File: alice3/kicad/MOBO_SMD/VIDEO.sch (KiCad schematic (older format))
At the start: 19 parts, among them P1 CONN_01X05, SW1 RESET, U2 Propeller_P8X32A-D40, U3 24LC256, U4 Propeller_Plug, Y1 5 MHz

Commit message: Unknown wiring changes automatically done by KiCAD in video board as a result of adding the EEPROM.
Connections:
- wire segments 134 -> 118
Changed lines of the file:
@@
 LIBS:mini_din
 LIBS:24lc256
+LIBS:MOBO_SMD-cache
 EELAYER 25 0
 EELAYER END
@@
 	3800 3550 3700 3550
 Wire Wire Line
-	3700 3550 3700 3650
-Wire Wire Line
-	3700 3650 3700 3850
+	3700 3550 3700 3850
 Wire Wire Line
 	3800 3650 3700 3650
@@
 	3700 1550 3800 1550
 Wire Wire Line
-	3700 1250 3700 1450
-Wire Wire Line
-	3700 1450 3700 1550
+	3700 1250 3700 1550
 Wire Wire Line
 	3800 1450 3700 1450
@@
 	5000 1550 5050 1550
 Wire Wire Line
-	5000 1450 5400 1450
-Wire Wire Line
-	5400 1450 5450 1450
-Wire Wire Line
-	5450 1450 5600 1450
+	5000 1450 5600 1450
 Wire Wire Line
 	3100 2650 3800 2650
@@
 	6000 3150 5950 3150
 Wire Wire Line
-	5950 3150 5950 3250
-Wire Wire Line
-	5950 3250 5950 3350
-Wire Wire Line
-	5950 3350 5950 3450
-Wire Wire Line
-	5950 3450 5950 3550
+	5950 3150 5950 3550
 Wire Wire Line
 	6000 3250 5950 3250
@@
 	7050 3450 7050 3850
 Wire Wire Line
-	7050 3850 5700 3850
-Wire Wire Line
-	5700 3850 5700 3150
-Wire Wire Line
-	5700 3150 5700 3100
+	5700 3850 7050 3850
+Wire Wire Line
+	5700 3100 5700 3850
 Wire Wire Line
 	5700 3150 5000 3150
@@
 	6850 1450 6850 1850
 Wire Wire Line
-	6200 1450 6250 1450
-Wire Wire Line
-	6250 1450 6850 1450
+	6200 1450 6850 1450
 Wire Wire Line
 	6250 1450 6250 1550
@@
 	3325 6225 3450 6225
 Wire Wire Line
-	3325 5725 3325 5825
-Wire Wire Line
-	3325 5825 3325 6225
-Wire Wire Line
-	3325 6225 3325 6425
-Wire Wire Line
-	3325 6425 3325 6625
-Wire Wire Line
-	3325 6625 3325 6775
+	3325 5725 3325 6775
 Wire Wire Line
 	3450 6425 3325 6425
@@
 	1800 6575 2325 6575
 Wire Wire Line
-	2325 6525 2325 6575
-Wire Wire Line
-	2325 6575 2325 6750
+	2325 6525 2325 6750
 Wire Wire Line
 	2325 6525 3450 6525
 Wire Wire Line
-	2325 6225 2325 6325
-Wire Wire Line
-	2325 6325 2325 6400
+	2325 6225 2325 6400
 Wire Wire Line
 	2325 6325 3450 6325
@@
 	1800 5875 2325 5875
 Wire Wire Line
-	2325 5875 2325 6050
-Wire Wire Line
-	2325 6050 2325 6125
+	2325 5875 2325 6125
 Wire Wire Line
 	2325 6400 1800 6400

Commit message: Fix up various small things.
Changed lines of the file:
@@
 	7050 3450 7050 3850
 Wire Wire Line
-	5700 3850 7050 3850
+	7050 3850 5700 3850
 Wire Wire Line
-	5700 3100 5700 3850
+	5700 3850 5700 3100
 Wire Wire Line
 	5700 3150 5000 3150

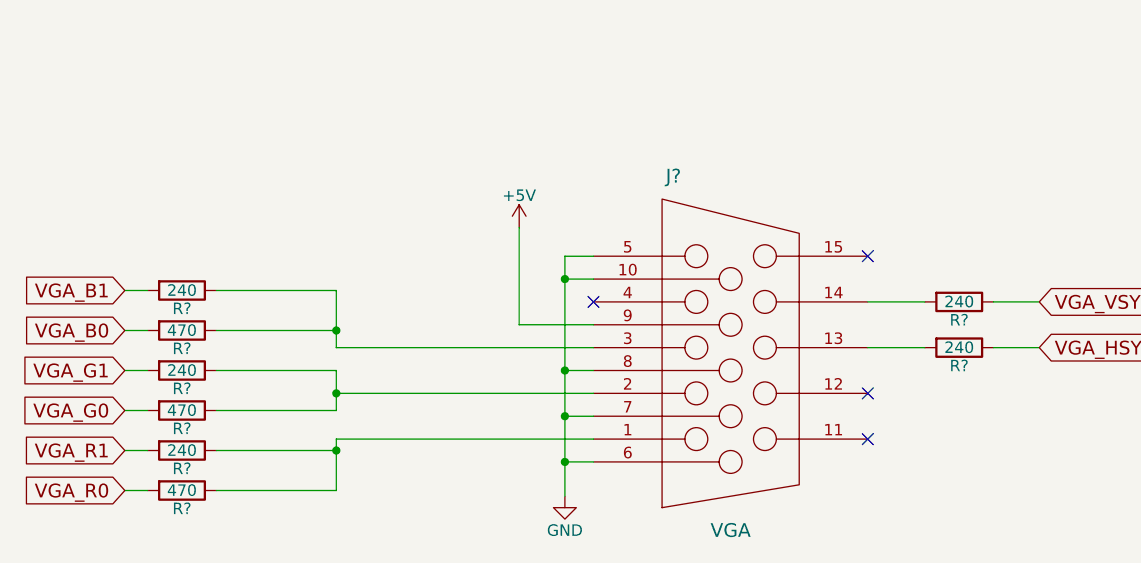
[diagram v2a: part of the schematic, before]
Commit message: Assign part names.
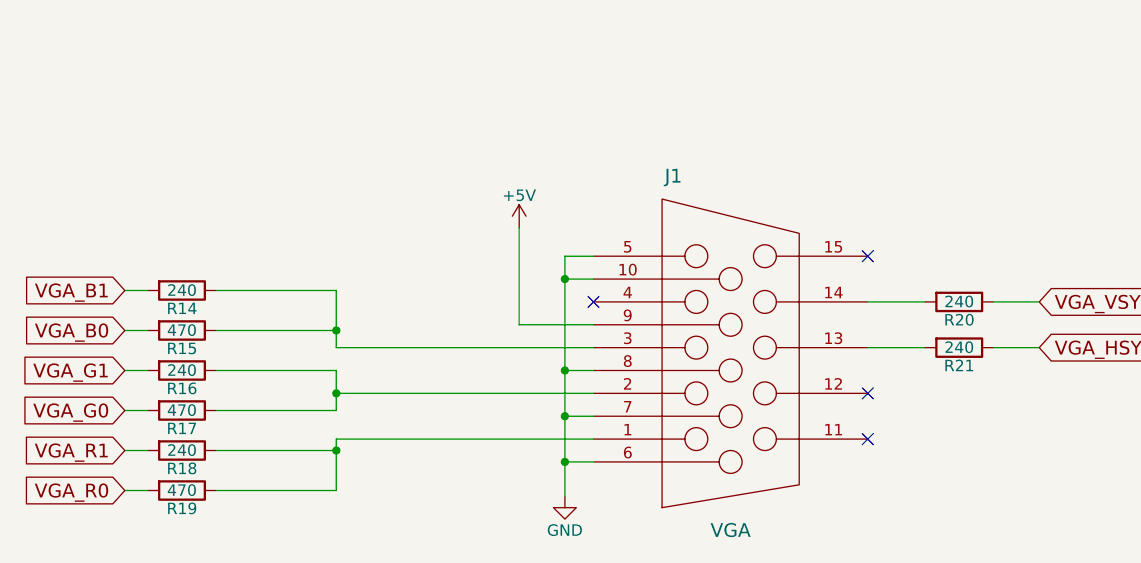
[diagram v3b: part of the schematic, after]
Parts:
- gave numbers to parts that had none: 9
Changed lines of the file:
@@
 $EndComp
 $Comp
-L GND #PWR01
+L GND #PWR9
 U 1 1 566E4A0D
 P 3700 3850
-F 0 "#PWR01" H 3700 3600 50  0001 C CNN
+F 0 "#PWR9" H 3700 3600 50  0001 C CNN
 F 1 "GND" H 3700 3700 50  0000 C CNN
 F 2 "" H 3700 3850 50  0000 C CNN
@@
 $EndComp
 $Comp
-L +3.3V #PWR02
+L +3.3V #PWR8
 U 1 1 566E4A37
 P 3700 1250
-F 0 "#PWR02" H 3700 1100 50  0001 C CNN
+F 0 "#PWR8" H 3700 1100 50  0001 C CNN
 F 1 "+3.3V" H 3700 1390 50  0000 C CNN
 F 2 "" H 3700 1250 50  0000 C CNN
@@
 $EndComp
 $Comp
-L GND #PWR03
+L GND #PWR13
 U 1 1 566E4C07
 P 6250 1550
-F 0 "#PWR03" H 6250 1300 50  0001 C CNN
+F 0 "#PWR13" H 6250 1300 50  0001 C CNN
 F 1 "GND" H 6250 1400 50  0000 C CNN
 F 2 "" H 6250 1550 50  0000 C CNN
@@
 $EndComp
 $Comp
-L GND #PWR04
+L GND #PWR12
 U 1 1 5681F164
 P 5950 3550
-F 0 "#PWR04" H 5950 3300 50  0001 C CNN
+F 0 "#PWR12" H 5950 3300 50  0001 C CNN
 F 1 "GND" H 5950 3400 50  0000 C CNN
 F 2 "" H 5950 3550 50  0000 C CNN
@@
 $EndComp
 $Comp
-L +3.3V #PWR05
+L +3.3V #PWR14
 U 1 1 5681F2C2
 P 7050 3000
-F 0 "#PWR05" H 7050 2850 50  0001 C CNN
+F 0 "#PWR14" H 7050 2850 50  0001 C CNN
 F 1 "+3.3V" H 7050 3140 50  0000 C CNN
 F 2 "" H 7050 3000 50  0000 C CNN
@@
 $EndComp
 $Comp
-L GND #PWR06
+L GND #PWR15
 U 1 1 5681F2E8
 P 7300 3300
-F 0 "#PWR06" H 7300 3050 50  0001 C CNN
+F 0 "#PWR15" H 7300 3050 50  0001 C CNN
 F 1 "GND" H 7300 3150 50  0000 C CNN
 F 2 "" H 7300 3300 50  0000 C CNN
@@
 $EndComp
 $Comp
-L +3.3V #PWR07
+L +3.3V #PWR11
 U 1 1 5681F435
 P 5700 2750
-F 0 "#PWR07" H 5700 2600 50  0001 C CNN
+F 0 "#PWR11" H 5700 2600 50  0001 C CNN
 F 1 "+3.3V" H 5700 2890 50  0000 C CNN
 F 2 "" H 5700 2750 50  0000 C CNN
@@
 $EndComp
 $Comp
-L GND #PWR08
+L GND #PWR3
 U 1 1 56821F3F
 P 2700 1850
-F 0 "#PWR08" H 2700 1600 50  0001 C CNN
+F 0 "#PWR3" H 2700 1600 50  0001 C CNN
 F 1 "GND" H 2700 1700 50  0000 C CNN
 F 2 "" H 2700 1850 50  0000 C CNN
@@
 $EndComp
 $Comp
-L GND #PWR09
+L GND #PWR10
 U 1 1 56826035
 P 5050 1550
-F 0 "#PWR09" H 5050 1300 50  0001 C CNN
+F 0 "#PWR10" H 5050 1300 50  0001 C CNN
 F 1 "GND" H 5050 1400 50  0000 C CNN
 F 2 "" H 5050 1550 50  0000 C CNN
@@
 $EndComp
 $Comp
-L GND #PWR012
+L GND #PWR7
 U 1 1 568DD571
 P 3400 1350
-F 0 "#PWR012" H 3400 1100 50  0001 C CNN
+F 0 "#PWR7" H 3400 1100 50  0001 C CNN
 F 1 "GND" H 3400 1200 50  0000 C CNN
 F 2 "" H 3400 1350 50  0000 C CNN
@@
 $EndComp
 $Comp
-L +3.3V #PWR013
+L +3.3V #PWR6
 U 1 1 568DD5A9
 P 3400 850
-F 0 "#PWR013" H 3400 700 50  0001 C CNN
+F 0 "#PWR6" H 3400 700 50  0001 C CNN
 F 1 "+3.3V" H 3400 990 50  0000 C CNN
 F 2 "" H 3400 850 50  0000 C CNN
@@
 $EndComp
 $Comp
-L GND #PWR014
+L GND #PWR1
 U 1 1 56A0506B
 P 1000 3050
-F 0 "#PWR014" H 1000 2800 50  0001 C CNN
+F 0 "#PWR1" H 1000 2800 50  0001 C CNN
 F 1 "GND" H 1000 2900 50  0000 C CNN
 F 2 "" H 1000 3050 50  0000 C CNN
@@
 $EndComp
 $Comp
-L +3.3V #PWR015
+L +3.3V #PWR2
 U 1 1 56A050A3
 P 1300 3050
-F 0 "#PWR015" H 1300 2900 50  0001 C CNN
+F 0 "#PWR2" H 1300 2900 50  0001 C CNN
 F 1 "+3.3V" H 1300 3190 50  0000 C CNN
 F 2 "" H 1300 3050 50  0000 C CNN
@@
 	1000 2950 1000 3050
 $Comp
-L VGA J?
+L VGA J1
 U 1 1 56CDDE3D
 P 4050 6175
-F 0 "J?" H 3800 6975 60  0000 C CNN
+F 0 "J1" H 3800 6975 60  0000 C CNN
 F 1 "VGA" H 4050 5425 60  0000 C CNN
 F 2 "" H 4050 6175 60  0000 C CNN
@@
 $EndComp
 $Comp
-L GND #PWR?
+L GND #PWR5
 U 1 1 56CDE065
 P 3325 6775
-F 0 "#PWR?" H 3325 6525 50  0001 C CNN
+F 0 "#PWR5" H 3325 6525 50  0001 C CNN
 F 1 "GND" H 3325 6625 50  0000 C CNN
 F 2 "" H 3325 6775 60  0000 C CNN
@@
 Connection ~ 3325 6625
 $Comp
-L +5V #PWR?
+L +5V #PWR4
 U 1 1 56CDE22E
 P 3125 5600
-F 0 "#PWR?" H 3125 5450 50  0001 C CNN
+F 0 "#PWR4" H 3125 5450 50  0001 C CNN
 F 1 "+5V" H 3125 5740 50  0000 C CNN
 F 2 "" H 3125 5600 60  0000 C CNN
@@
 VGA_HSYNC
 $Comp
-L R R?
+L R R20
 U 1 1 56CDE76C
 P 5050 5925
-F 0 "R?" V 5130 5925 50  0000 C CNN
+F 0 "R20" V 5130 5925 50  0000 C CNN
 F 1 "240" V 5050 5925 50  0000 C CNN
 F 2 "" V 4980 5925 30  0000 C CNN
@@
 $EndComp
 $Comp
-L R R?
+L R R21
 U 1 1 56CDE802
 P 5050 6125
-F 0 "R?" V 5130 6125 50  0000 C CNN
+F 0 "R21" V 5130 6125 50  0000 C CNN
 F 1 "240" V 5050 6125 50  0000 C CNN
 F 2 "" V 4980 6125 30  0000 C CNN
@@
 VGA_R1
 $Comp
-L R R?
+L R R18
 U 1 1 56CDEB62
 P 1650 6575
-F 0 "R?" V 1730 6575 50  0000 C CNN
+F 0 "R18" V 1730 6575 50  0000 C CNN
 F 1 "240" V 1650 6575 50  0000 C CNN
 F 2 "" V 1580 6575 30  0000 C CNN
@@
 $EndComp
 $Comp
-L R R?
+L R R19
 U 1 1 56CDEBBE
 P 1650 6750
-F 0 "R?" V 1730 6750 50  0000 C CNN
+F 0 "R19" V 1730 6750 50  0000 C CNN
 F 1 "470" V 1650 6750 50  0000 C CNN
 F 2 "" V 1580 6750 30  0000 C CNN
@@
 VGA_G1
 $Comp
-L R R?
+L R R16
 U 1 1 56CDF048
 P 1650 6225
-F 0 "R?" V 1730 6225 50  0000 C CNN
+F 0 "R16" V 1730 6225 50  0000 C CNN
 F 1 "240" V 1650 6225 50  0000 C CNN
 F 2 "" V 1580 6225 30  0000 C CNN
@@
 $EndComp
 $Comp
-L R R?
+L R R17
 U 1 1 56CDF04E
 P 1650 6400
-F 0 "R?" V 1730 6400 50  0000 C CNN
+F 0 "R17" V 1730 6400 50  0000 C CNN
 F 1 "470" V 1650 6400 50  0000 C CNN
 F 2 "" V 1580 6400 30  0000 C CNN
@@
 VGA_B1
 $Comp
-L R R?
+L R R14
 U 1 1 56CDF0F4
 P 1650 5875
-F 0 "R?" V 1730 5875 50  0000 C CNN
+F 0 "R14" V 1730 5875 50  0000 C CNN
 F 1 "240" V 1650 5875 50  0000 C CNN
 F 2 "" V 1580 5875 30  0000 C CNN
@@
 $EndComp
 $Comp
-L R R?
+L R R15
 U 1 1 56CDF0FA
 P 1650 6050
-F 0 "R?" V 1730 6050 50  0000 C CNN
+F 0 "R15" V 1730 6050 50  0000 C CNN
 F 1 "470" V 1650 6050 50  0000 C CNN
 F 2 "" V 1580 6050 30  0000 C CNN

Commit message: Replace Propeller with Q44 version. Remove Prop debug LED.
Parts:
- removed D1: DEBUG, LEDs:LED_0805, symbol LED
- removed R1: 100, Resistors_SMD:R_0805, symbol R
- removed U2: Propeller_P8X32A-D40, Housings_QFP:LQFP-44_10x10mm_Pitch0.8mm, symbol Propeller_P8X32A-D40
- added U2: Propeller_P8X32A-Q44, symbol Propeller_P8X32A-Q44
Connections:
- wire segments 118 -> 120
- no-connect marks 4 -> 5
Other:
- moved on the sheet: C1
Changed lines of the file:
@@
 LIBS:24lc256
 LIBS:z80cpu-smd
+LIBS:propeller_p8x32a-q44
 LIBS:MOBO_SMD-cache
 EELAYER 25 0
@@
 $EndDescr
 $Comp
-L Propeller_P8X32A-D40 U2
-U 1 1 566E498F
-P 4400 2550
-F 0 "U2" H 4100 3850 60  0000 C CNN
-F 1 "Propeller_P8X32A-D40" H 4400 1250 60  0000 C CNN
-F 2 "Housings_QFP:LQFP-44_10x10mm_Pitch0.8mm" H 4400 2350 60  0001 C CNN
-F 3 "" H 4400 2350 60  0000 C CNN
-	1    4400 2550
-	1    0    0    -1
-$EndComp
-$Comp
-L GND #PWR9
+L GND #PWR7
 U 1 1 566E4A0D
-P 3700 3850
-F 0 "#PWR9" H 3700 3600 50  0001 C CNN
-F 1 "GND" H 3700 3700 50  0000 C CNN
-F 2 "" H 3700 3850 50  0000 C CNN
-F 3 "" H 3700 3850 50  0000 C CNN
-	1    3700 3850
-	1    0    0    -1
-$EndComp
-$Comp
-L +3.3V #PWR8
+P 3700 3900
+F 0 "#PWR7" H 3700 3650 50  0001 C CNN
+F 1 "GND" H 3700 3750 50  0000 C CNN
+F 2 "" H 3700 3900 50  0000 C CNN
+F 3 "" H 3700 3900 50  0000 C CNN
+	1    3700 3900
+	1    0    0    -1
+$EndComp
+$Comp
+L +3.3V #PWR6
 U 1 1 566E4A37
-P 3700 1250
-F 0 "#PWR8" H 3700 1100 50  0001 C CNN
-F 1 "+3.3V" H 3700 1390 50  0000 C CNN
-F 2 "" H 3700 1250 50  0000 C CNN
-F 3 "" H 3700 1250 50  0000 C CNN
-	1    3700 1250
+P 3700 900
+F 0 "#PWR6" H 3700 750 50  0001 C CNN
+F 1 "+3.3V" H 3700 1040 50  0000 C CNN
+F 2 "" H 3700 900 50  0000 C CNN
+F 3 "" H 3700 900 50  0000 C CNN
+	1    3700 900
 	1    0    0    -1
 $EndComp
@@
 $EndComp
 $Comp
-L GND #PWR13
+L GND #PWR11
 U 1 1 566E4C07
 P 6250 1550
-F 0 "#PWR13" H 6250 1300 50  0001 C CNN
+F 0 "#PWR11" H 6250 1300 50  0001 C CNN
 F 1 "GND" H 6250 1400 50  0000 C CNN
 F 2 "" H 6250 1550 50  0000 C CNN
@@
 $EndComp
 $Comp
-L GND #PWR12
+L GND #PWR10
 U 1 1 5681F164
 P 5950 3550
-F 0 "#PWR12" H 5950 3300 50  0001 C CNN
+F 0 "#PWR10" H 5950 3300 50  0001 C CNN
 F 1 "GND" H 5950 3400 50  0000 C CNN
 F 2 "" H 5950 3550 50  0000 C CNN
@@
 $EndComp
 $Comp
-L +3.3V #PWR14
+L +3.3V #PWR12
 U 1 1 5681F2C2
 P 7050 3000
-F 0 "#PWR14" H 7050 2850 50  0001 C CNN
+F 0 "#PWR12" H 7050 2850 50  0001 C CNN
 F 1 "+3.3V" H 7050 3140 50  0000 C CNN
 F 2 "" H 7050 3000 50  0000 C CNN
@@
 $EndComp
 $Comp
-L GND #PWR15
+L GND #PWR13
 U 1 1 5681F2E8
 P 7300 3300
-F 0 "#PWR15" H 7300 3050 50  0001 C CNN
+F 0 "#PWR13" H 7300 3050 50  0001 C CNN
 F 1 "GND" H 7300 3150 50  0000 C CNN
 F 2 "" H 7300 3300 50  0000 C CNN
@@
 $EndComp
 $Comp
-L +3.3V #PWR11
+L +3.3V #PWR9
 U 1 1 5681F435
 P 5700 2750
-F 0 "#PWR11" H 5700 2600 50  0001 C CNN
+F 0 "#PWR9" H 5700 2600 50  0001 C CNN
 F 1 "+3.3V" H 5700 2890 50  0000 C CNN
 F 2 "" H 5700 2750 50  0000 C CNN
@@
 $EndComp
 $Comp
-L LED D1
-U 1 1 56821EAA
-P 3300 1750
-F 0 "D1" H 3300 1850 50  0000 C CNN
-F 1 "DEBUG" H 3300 1650 50  0000 C CNN
-F 2 "LEDs:LED_0805" H 3300 1750 50  0001 C CNN
-F 3 "" H 3300 1750 50  0000 C CNN
-	1    3300 1750
-	1    0    0    -1
-$EndComp
-$Comp
-L R R1
-U 1 1 56821F00
-P 2850 1750
-F 0 "R1" V 2930 1750 50  0000 C CNN
-F 1 "100" V 2850 1750 50  0000 C CNN
-F 2 "Resistors_SMD:R_0805" V 2780 1750 50  0001 C CNN
-F 3 "" H 2850 1750 50  0000 C CNN
-	1    2850 1750
-	0    1    1    0
-$EndComp
-$Comp
-L GND #PWR3
-U 1 1 56821F3F
-P 2700 1850
-F 0 "#PWR3" H 2700 1600 50  0001 C CNN
-F 1 "GND" H 2700 1700 50  0000 C CNN
-F 2 "" H 2700 1850 50  0000 C CNN
-F 3 "" H 2700 1850 50  0000 C CNN
-	1    2700 1850
-	1    0    0    -1
-$EndComp
-$Comp
-L GND #PWR10
+L GND #PWR8
 U 1 1 56826035
 P 5050 1550
-F 0 "#PWR10" H 5050 1300 50  0001 C CNN
+F 0 "#PWR8" H 5050 1300 50  0001 C CNN
 F 1 "GND" H 5050 1400 50  0000 C CNN
 F 2 "" H 5050 1550 50  0000 C CNN
@@
 	3800 3550 3700 3550
 Wire Wire Line
-	3700 3550 3700 3850
+	3700 3550 3700 3900
 Wire Wire Line
 	3800 3650 3700 3650
@@
 	3700 1550 3800 1550
 Wire Wire Line
-	3700 1250 3700 1550
+	3700 900  3700 1550
 Wire Wire Line
 	3800 1450 3700 1450
@@
 	6250 1450 6250 1550
 Connection ~ 6250 1450
-Wire Wire Line
-	3500 1750 3800 1750
 Wire Wire Line
 	5000 1750 5100 1750
@@
 L C C1
 U 1 1 568DD525
-P 3400 1100
-F 0 "C1" H 3425 1200 50  0000 L CNN
-F 1 "0.1 µF" H 3425 1000 50  0000 L CNN
-F 2 "Capacitors_SMD:C_0805" H 3438 950 50  0001 C CNN
-F 3 "" H 3400 1100 50  0000 C CNN
-	1    3400 1100
-	1    0    0    -1
-$EndComp
-$Comp
-L GND #PWR7
+P 3400 1150
+F 0 "C1" H 3425 1250 50  0000 L CNN
+F 1 "0.1 µF" H 3425 1050 50  0000 L CNN
+F 2 "Capacitors_SMD:C_0805" H 3438 1000 50  0001 C CNN
+F 3 "" H 3400 1150 50  0000 C CNN
+	1    3400 1150
+	1    0    0    -1
+$EndComp
+$Comp
+L GND #PWR5
 U 1 1 568DD571
-P 3400 1350
-F 0 "#PWR7" H 3400 1100 50  0001 C CNN
-F 1 "GND" H 3400 1200 50  0000 C CNN
-F 2 "" H 3400 1350 50  0000 C CNN
-F 3 "" H 3400 1350 50  0000 C CNN
-	1    3400 1350
-	1    0    0    -1
-$EndComp
-$Comp
-L +3.3V #PWR6
-U 1 1 568DD5A9
-P 3400 850
-F 0 "#PWR6" H 3400 700 50  0001 C CNN
-F 1 "+3.3V" H 3400 990 50  0000 C CNN
-F 2 "" H 3400 850 50  0000 C CNN
-F 3 "" H 3400 850 50  0000 C CNN
-	1    3400 850
-	1    0    0    -1
-$EndComp
-Wire Wire Line
-	3400 850  3400 950
-Wire Wire Line
-	3400 1250 3400 1350
+P 3400 1400
+F 0 "#PWR5" H 3400 1150 50  0001 C CNN
+F 1 "GND" H 3400 1250 50  0000 C CNN
+F 2 "" H 3400 1400 50  0000 C CNN
+F 3 "" H 3400 1400 50  0000 C CNN
+	1    3400 1400
+	1    0    0    -1
+$EndComp
 Text GLabel 3800 2250 0    60   Output ~ 0
 CLK
@@
 	5450 1650 5450 1450
 Connection ~ 5450 1450
-Wire Wire Line
-	3100 1750 3000 1750
-Wire Wire Line
-	2700 1750 2700 1850
 Wire Wire Line
 	3800 2350 1100 2350
@@
 $EndComp
 $Comp
-L GND #PWR5
+L GND #PWR4
 U 1 1 56CDE065
 P 3325 6775
-F 0 "#PWR5" H 3325 6525 50  0001 C CNN
+F 0 "#PWR4" H 3325 6525 50  0001 C CNN
 F 1 "GND" H 3325 6625 50  0000 C CNN
 F 2 "" H 3325 6775 60  0000 C CNN
@@
 Connection ~ 3325 6625
 $Comp
-L +5V #PWR4
+L +5V #PWR3
 U 1 1 56CDE22E
 P 3125 5600
-F 0 "#PWR4" H 3125 5450 50  0001 C CNN
+F 0 "#PWR3" H 3125 5450 50  0001 C CNN
 F 1 "+5V" H 3125 5740 50  0000 C CNN
 F 2 "" H 3125 5600 60  0000 C CNN
@@
 Text GLabel 3100 3350 0    60   Output ~ 0
 VGA_R0
+$Comp
+L Propeller_P8X32A-Q44 U2
+U 1 1 56D3996F
+P 4400 2550
+F 0 "U2" H 4100 4050 60  0000 C CNN
+F 1 "Propeller_P8X32A-Q44" H 4450 1050 60  0000 C CNN
+F 2 "" H 4400 2350 60  0000 C CNN
+F 3 "" H 4400 2350 60  0000 C CNN
+	1    4400 2550
+	1    0    0    -1
+$EndComp
+Wire Wire Line
+	3800 3850 3700 3850
+Connection ~ 3700 3850
+Wire Wire Line
+	3800 3750 3700 3750
+Connection ~ 3700 3750
+Wire Wire Line
+	3700 1250 3800 1250
+Connection ~ 3700 1250
+Wire Wire Line
+	3700 1350 3800 1350
+Connection ~ 3700 1350
+Wire Wire Line
+	3400 1400 3400 1300
+Wire Wire Line
+	3400 1000 3400 950
+Wire Wire Line
+	3400 950  3700 950
+Connection ~ 3700 950
+NoConn ~ 3800 1750
 $EndSCHEMATC

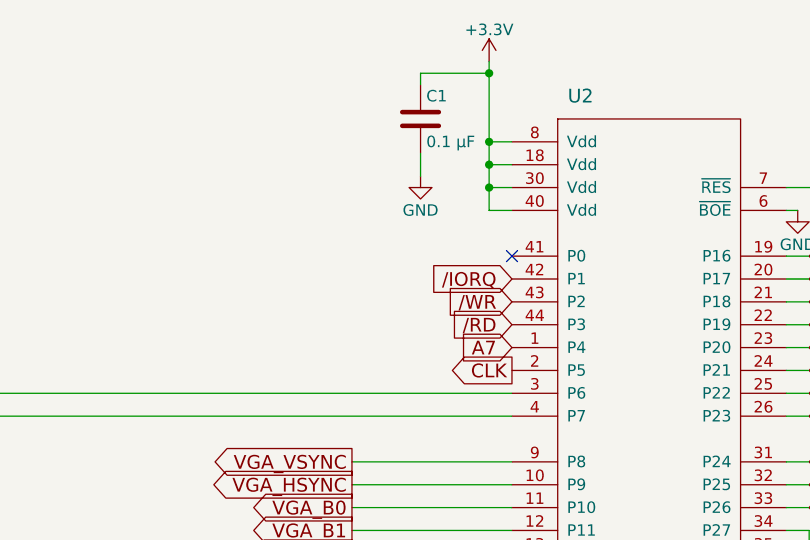
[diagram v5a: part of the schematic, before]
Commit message: Add PROP_READY line; add A17 to ARM.
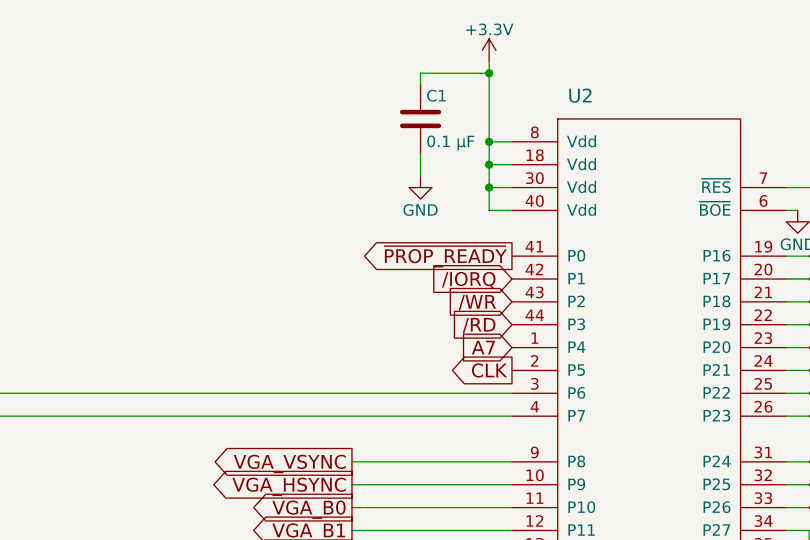
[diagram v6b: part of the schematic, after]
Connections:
- net labels added: ~PROP_READY~
- no-connect marks 5 -> 4
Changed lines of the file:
@@
 	3400 950  3700 950
 Connection ~ 3700 950
-NoConn ~ 3800 1750
+Text GLabel 3800 1750 0    60   Output ~ 0
+~PROP_READY~
 $EndSCHEMATC
